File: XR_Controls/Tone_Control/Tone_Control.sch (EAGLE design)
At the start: 5 parts

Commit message: Licenses
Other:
- note added: "Tone Control Project by Cycfi Research is licensed under a Creative Commons Attribution-ShareAlike 4.0 International License. http://creativecommons.org/licenses/by-sa/4.0/ Copyright CYCFI Research Inc. 2013-2016"
- note removed: "XR Controls Project by Cycfi Research is licensed under a Creative Commons Attribution-NonCommercial 4.0 International License. http://creativecommons.org/licenses/by-nc/4.0/ Copyright CYCFI Research Inc. 2013-2016"
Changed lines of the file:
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@@
 <text x="177.8" y="19.05" size="2.54" layer="95">Tone Control</text>
 <text x="253.365" y="6.985" size="2.1844" layer="95">v1.46</text>
-<text x="7.62" y="12.7" size="2.54" layer="95">XR Controls Project by Cycfi Research is licensed under a
-Creative Commons Attribution-NonCommercial 4.0 International License.
-http://creativecommons.org/licenses/by-nc/4.0/
+<text x="7.62" y="12.7" size="2.54" layer="95">Tone Control Project by Cycfi Research is licensed under a Creative
+Commons Attribution-ShareAlike 4.0 International License.
+http://creativecommons.org/licenses/by-sa/4.0/
 Copyright CYCFI Research Inc. 2013-2016</text>
 <text x="200.66" y="11.43" size="2.54" layer="95">2016040</text>

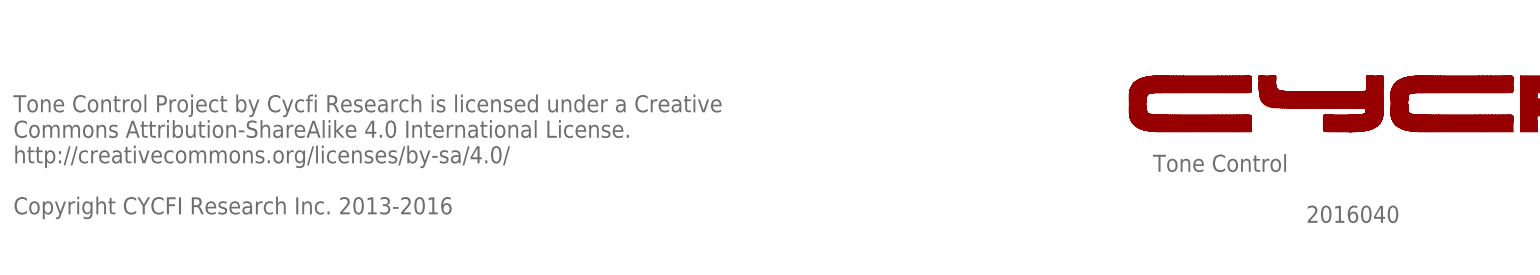
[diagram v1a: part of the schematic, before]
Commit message: *organize 5-waay switch and its configuration board(a and b) *update license date *remove red frame schem pdf files, change with black frame *update document number
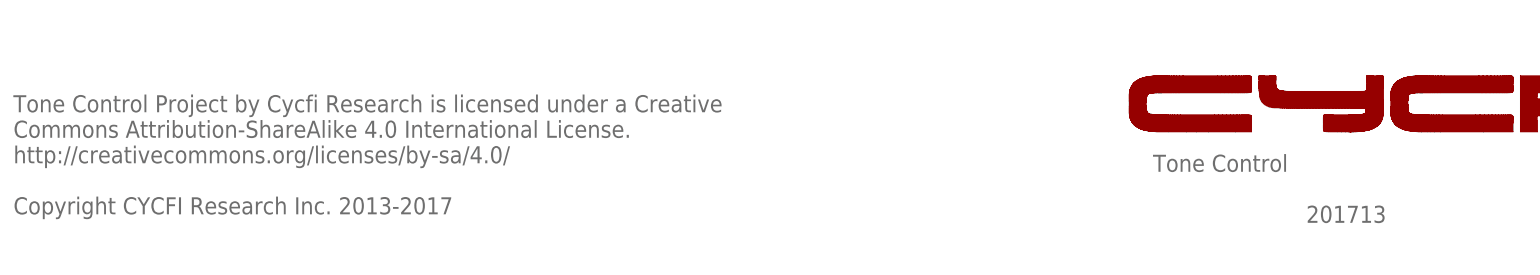
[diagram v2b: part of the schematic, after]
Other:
- note added: "201713"
- note added: "Tone Control Project by Cycfi Research is licensed under a Creative Commons Attribution-ShareAlike 4.0 International License. http://creativecommons.org/licenses/by-sa/4.0/ Copyright CYCFI Research Inc. 2013-2017"
- note removed: "2016040"
- note removed: "Tone Control Project by Cycfi Research is licensed under a Creative Commons Attribution-ShareAlike 4.0 International License. http://creativecommons.org/licenses/by-sa/4.0/ Copyright CYCFI Research Inc. 2013-2016"
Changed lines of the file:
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@@
 Commons Attribution-ShareAlike 4.0 International License.
 http://creativecommons.org/licenses/by-sa/4.0/
-Copyright CYCFI Research Inc. 2013-2016</text>
-<text x="200.66" y="11.43" size="2.54" layer="95">2016040</text>
+Copyright CYCFI Research Inc. 2013-2017</text>
+<text x="200.66" y="11.43" size="2.54" layer="95">201713</text>
 <wire x1="192.47528125" y1="25.047221875" x2="190.115640625" y2="25.047221875" width="0" layer="94"/>
 <wire x1="190.115640625" y1="25.047221875" x2="188.10833125" y2="25.047225" width="0" layer="94"/>

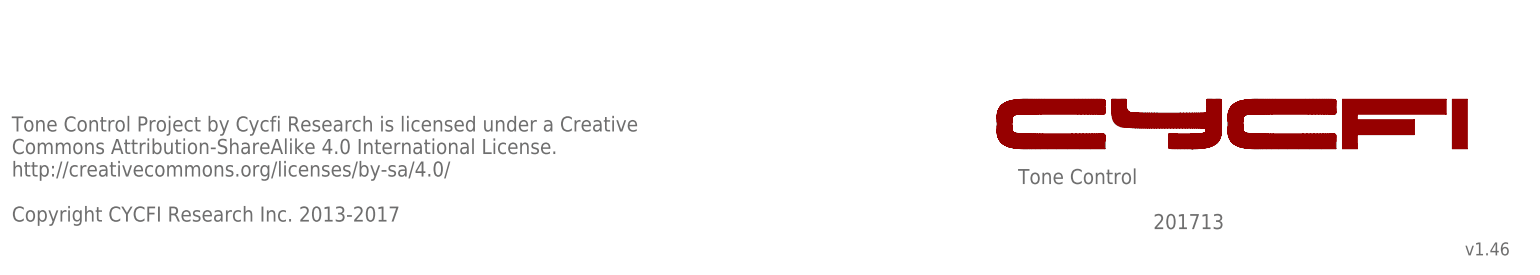
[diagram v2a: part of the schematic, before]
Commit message: Updated broken .sch files
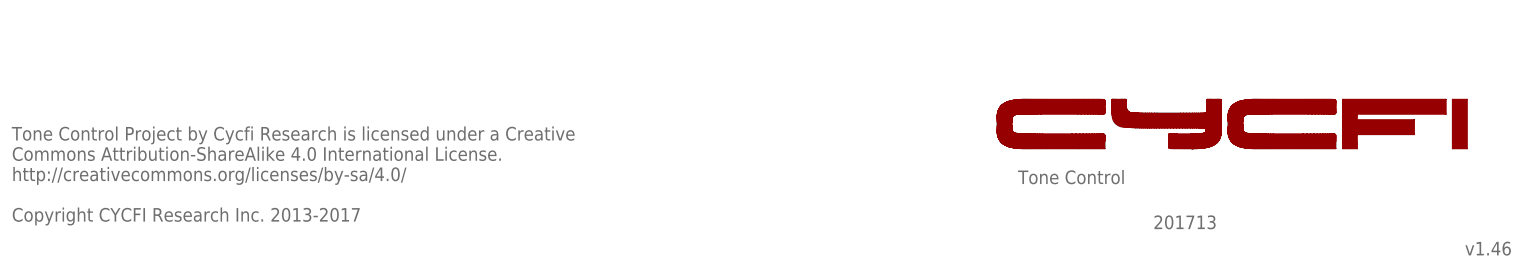
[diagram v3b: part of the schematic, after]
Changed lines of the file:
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@@
 <text x="106.68" y="111.76" size="1.778" layer="95">POT1
 25K</text>
-<text x="177.8" y="19.05" size="2.54" layer="95">Tone Control</text>
-<text x="253.365" y="6.985" size="2.1844" layer="95">v1.46</text>
-<text x="7.62" y="12.7" size="2.54" layer="95">Tone Control Project by Cycfi Research is licensed under a Creative
+<text x="177.8" y="19.05" size="2.286" layer="95" font="vector">Tone Control</text>
+<text x="253.365" y="6.985" size="2.286" layer="95" font="vector">v1.46</text>
+<text x="7.62" y="12.7" size="2.286" layer="95" font="vector">Tone Control Project by Cycfi Research is licensed under a Creative
 Commons Attribution-ShareAlike 4.0 International License.
 http://creativecommons.org/licenses/by-sa/4.0/
 Copyright CYCFI Research Inc. 2013-2017</text>
-<text x="200.66" y="11.43" size="2.54" layer="95">201713</text>
+<text x="200.66" y="11.43" size="2.286" layer="95" font="vector">201713</text>
 <wire x1="192.47528125" y1="25.047221875" x2="190.115640625" y2="25.047221875" width="0" layer="94"/>
 <wire x1="190.115640625" y1="25.047221875" x2="188.10833125" y2="25.047225" width="0" layer="94"/>
@@
 <instance part="FRAME1" gate="G$1" x="0" y="0"/>
 <instance part="FRAME1" gate="G$2" x="162.56" y="0" smashed="yes">
-<attribute name="LAST_DATE_TIME" x="175.26" y="1.27" size="2.54" layer="94" font="vector"/>
-<attribute name="SHEET" x="248.92" y="1.27" size="2.54" layer="94" font="vector"/>
+<attribute name="LAST_DATE_TIME" x="175.26" y="1.27" size="2.286" layer="94" font="vector"/>
+<attribute name="SHEET" x="248.92" y="1.27" size="2.286" layer="94" font="vector"/>
 </instance>
 </instances>
